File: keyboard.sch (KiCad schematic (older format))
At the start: 49 parts, among them J1 HRO_TYPE-C-31-M-12, J2 HRO_TYPE-C-31-M-12, J3 M55-7101642R, J4 M55-6101642R, SW1 P830, U1 USBLC6-2P6, U2 USBLC6-2P6, U3 MIC5504-3.3YM5, U4 STM32F042K6Ux, U5 USB2422-MJ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

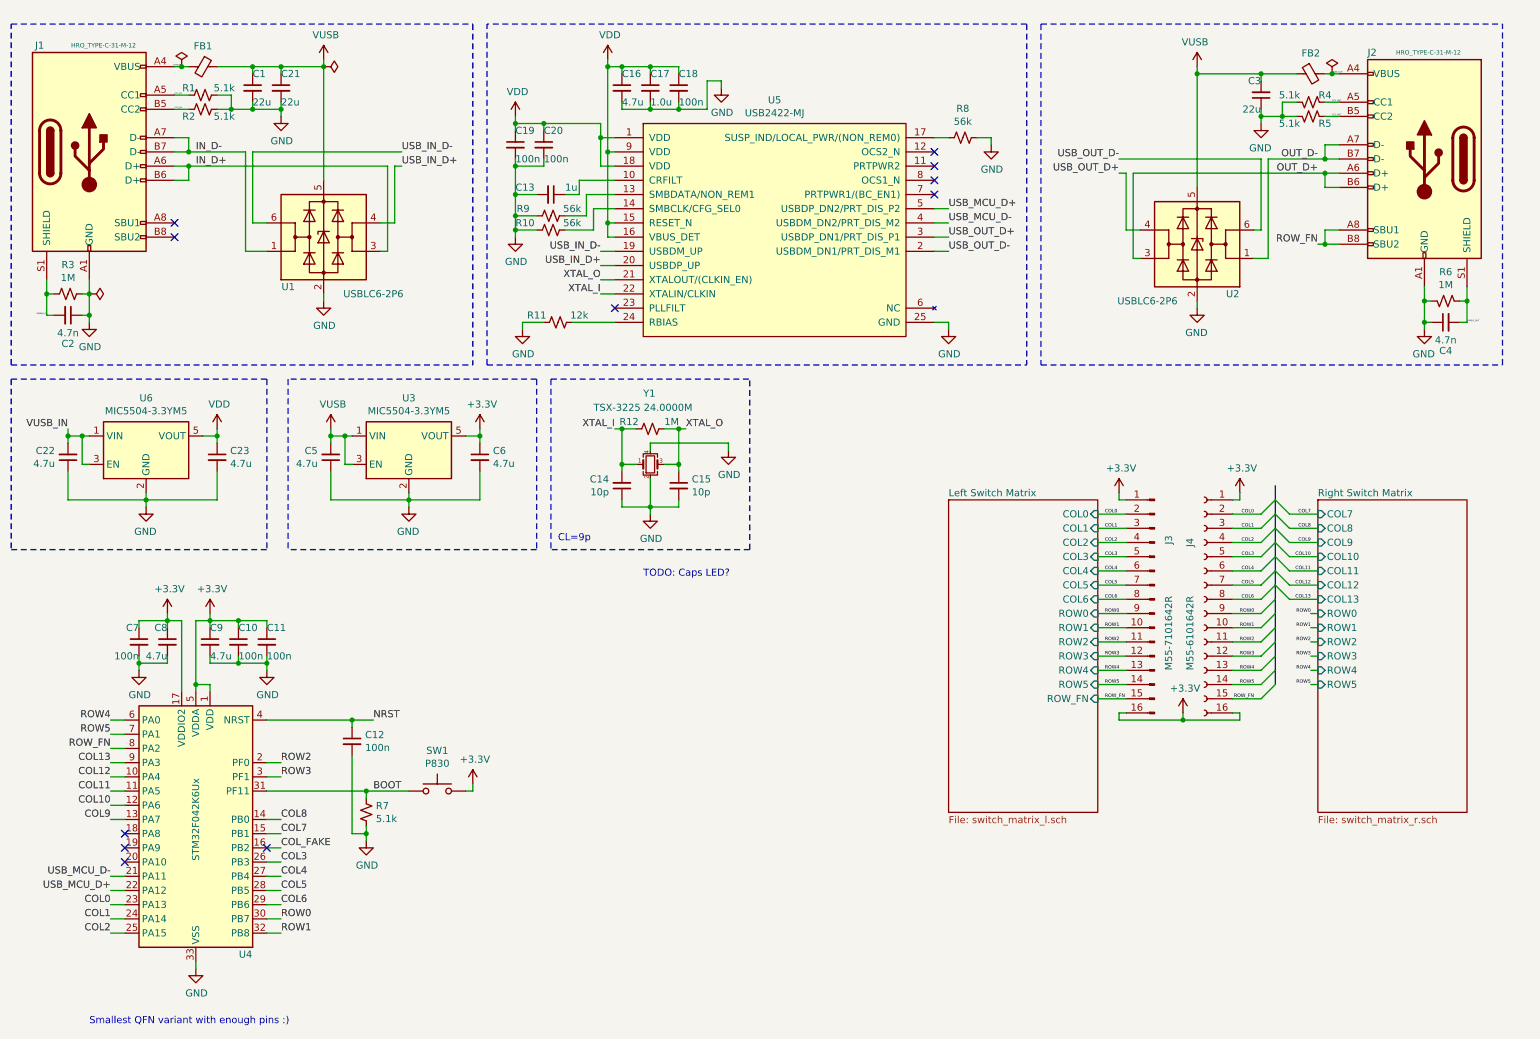
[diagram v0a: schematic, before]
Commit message: Add TODO notes to schematic
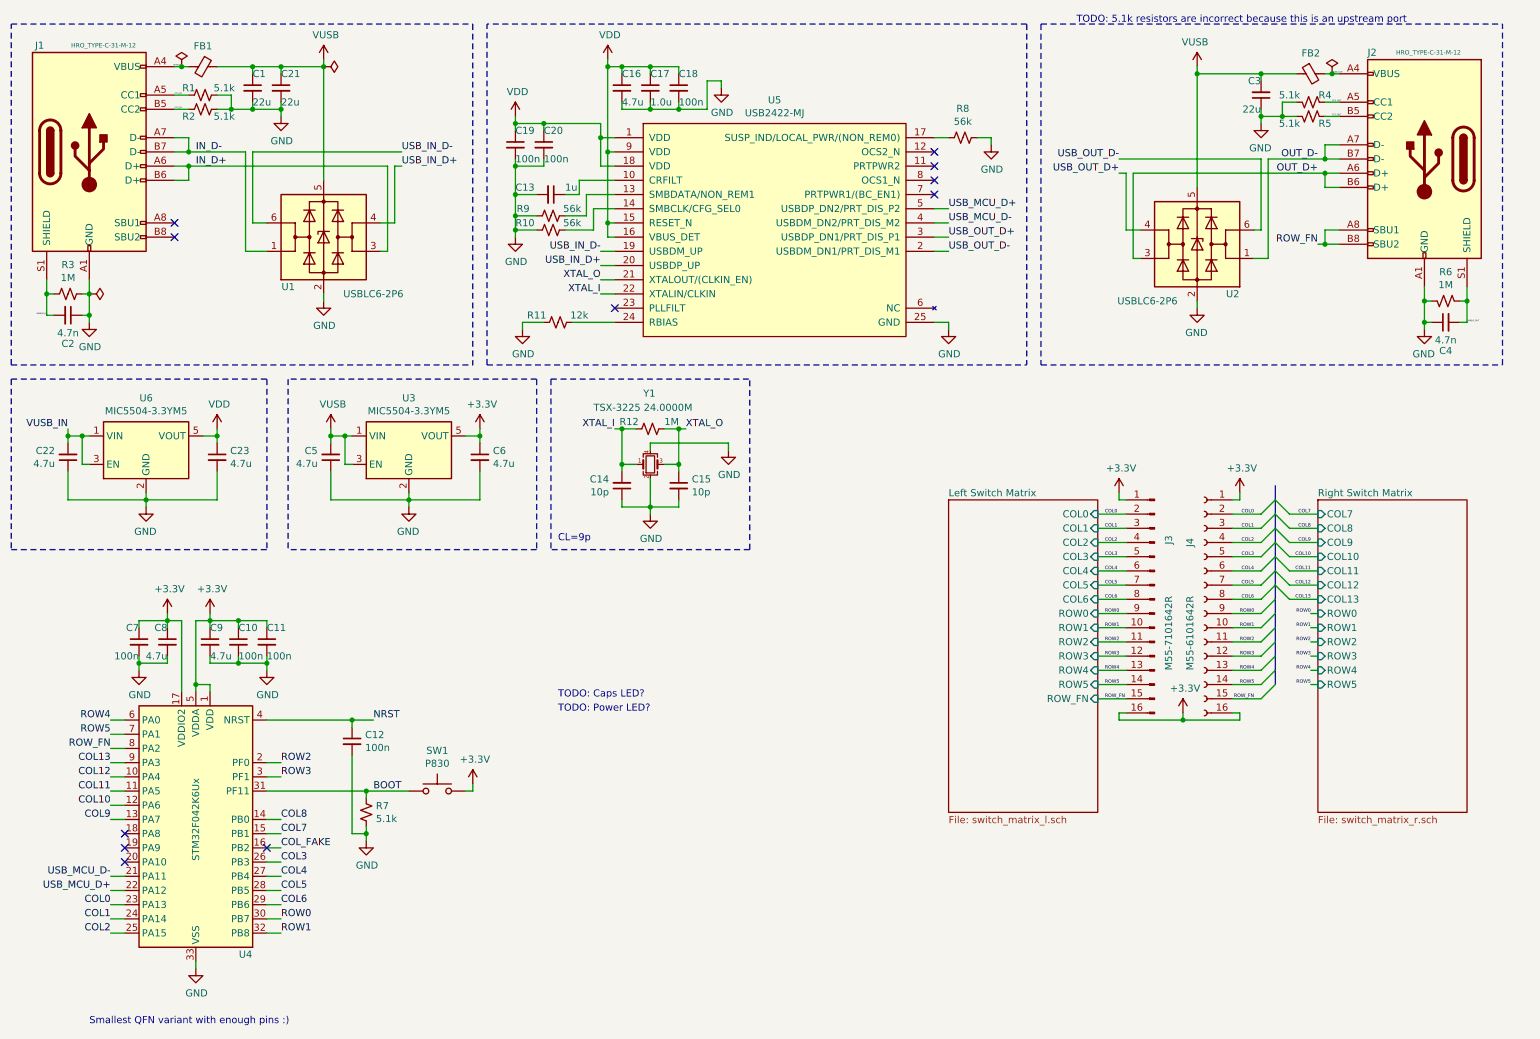
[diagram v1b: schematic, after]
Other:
- note added: "TODO: 5.1k resistors are incorrect because this is an upstream port"
- note added: "TODO: Power LED?"
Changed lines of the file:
@@
 	9400 950  9650 950
 Connection ~ 2500 1200
-Text Notes 5050 4500 0    50   ~ 0
+Text Notes 4450 5350 0    50   ~ 0
 TODO: Caps LED?
 Wire Wire Line
@@
 	1    0    0    -1
 $EndComp
+Text Notes 8100 600  0    50   ~ 0
+TODO: 5.1k resistors are incorrect because this is an upstream port
 Wire Bus Line
 	9500 3850 9500 5250
+Text Notes 4450 5450 0    50   ~ 0
+TODO: Power LED?
 $EndSCHEMATC
